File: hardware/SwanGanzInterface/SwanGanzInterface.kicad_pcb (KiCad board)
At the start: 2 copper layers, 27 parts, among them IC2 LM2937ET-3.3_NOPB, J1 2479774-1, Q1 SQ2389CES-T1_GE3, SW1 Power_Switch, U1 INA122D, U10 OPA2350, U2 OPA2350, U3 OPA2350, U4 INA122D, U5 OPA2350, U6 INA122D, U8 Adafruit ST7735R

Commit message: Footprints for most parts, added LCD Driver
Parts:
- added C1: 0.1u, Capacitor_SMD:C_0603_1608Metric, F.Cu at (250.4, 240.2)
- added C11: 0.1u, Capacitor_SMD:C_0603_1608Metric, F.Cu at (250.4, 228.2)
- added C12: 0.1u, Capacitor_SMD:C_1206_3216Metric, F.Cu at (267.8, 228.6)
- added C13: 0.1u, Capacitor_SMD:C_0603_1608Metric, F.Cu at (250.4, 230.7)
- added C15: 0.1u, Capacitor_SMD:C_1206_3216Metric, F.Cu at (255.2, 184.5)
- added C16: 0.1u, Capacitor_SMD:C_1206_3216Metric, F.Cu at (255.2, 187.8)
- added C17: 0.1u, Capacitor_SMD:C_0603_1608Metric, F.Cu at (250.4, 176.8)
- added C19: 0.1u, Capacitor_SMD:C_1206_3216Metric, F.Cu at (255.2, 206.5)
- added C2: 10u, Capacitor_SMD:C_1206_3216Metric, F.Cu at (255.2, 240.7)
- added C20: 0.1u, Capacitor_SMD:C_1206_3216Metric, F.Cu at (255.2, 209.9)
- added C21: 0.1u, Capacitor_SMD:C_0603_1608Metric, F.Cu at (250.4, 198.9)
- added C3: 0.1u, Capacitor_SMD:C_0603_1608Metric, F.Cu at (250.4, 242.8)
- added C4: 0.1u, Capacitor_SMD:C_0603_1608Metric, F.Cu at (95.7, 251.4)
- added C5: 0.1u, Capacitor_SMD:C_0603_1608Metric, F.Cu at (266.1, 140.6)
- added C6: 0.1u, Capacitor_SMD:C_0603_1608Metric, F.Cu at (95.7, 253.9)
- added C7: 0.1u, Capacitor_SMD:C_0603_1608Metric, F.Cu at (266.1, 143.1)
- added C8: 0.1u, Capacitor_SMD:C_0603_1608Metric, F.Cu at (221.3, 205.6)
- added C9: 0.1u, Capacitor_SMD:C_0603_1608Metric, F.Cu at (221.3, 208.1)
- added J2: Conn_01x08_Pin, Connector_PinHeader_2.54mm:PinHeader_1x08_P2.54mm_Vertical, F.Cu at (176.0, 75.3)
- added J3: Conn_01x03_Pin, Connector_PinHeader_2.54mm:PinHeader_1x03_P2.54mm_Vertical, F.Cu at (246.3, 145.0)
- added J6: Conn_01x04_Pin, Connector_PinSocket_2.54mm:PinSocket_1x04_P2.54mm_Vertical, F.Cu at (127.5, 223.5)
- added J7: Conn_01x04_Pin, Connector_PinSocket_2.54mm:PinSocket_1x04_P2.54mm_Vertical, F.Cu at (134.1, 223.5)
- added JP1: LP_3V3_Jumper, SGI_FootprintsLib:PinHeader_1x02_P2.54mm_Vertical, F.Cu at (221.6, 199.4)
- added JP2: LP_5V_Jumper, SGI_FootprintsLib:PinHeader_1x02_P2.54mm_Vertical, F.Cu at (226.3, 199.4)
- added JP3: FT232_3V3_Jumper, SGI_FootprintsLib:PinHeader_1x02_P2.54mm_Vertical, F.Cu at (230.9, 199.4)
- added R1: 5k1, Resistor_SMD:R_0603_1608Metric, F.Cu at (250.4, 245.3)
- added R10: 100R, Resistor_SMD:R_0603_1608Metric, F.Cu at (266.1, 148.1)
- added R11: 0R, Resistor_SMD:R_0603_1608Metric, F.Cu at (215.8, 209.7)
- added R12: 0R, Resistor_SMD:R_0603_1608Metric, F.Cu at (215.8, 212.2)
- added R13: 100k, Resistor_SMD:R_0603_1608Metric, F.Cu at (266.1, 150.7)
- added R14: 100R, Resistor_SMD:R_0603_1608Metric, F.Cu at (266.1, 153.2)
- added R15: 100k, Resistor_SMD:R_0603_1608Metric, F.Cu at (250.4, 233.2)
- added R16: 8k2, Resistor_SMD:R_0603_1608Metric, F.Cu at (250.4, 235.7)
- added R17: 100k, Resistor_SMD:R_0603_1608Metric, F.Cu at (254.4, 228.2)
- added R18: 65k5, Resistor_SMD:R_0603_1608Metric, F.Cu at (254.4, 230.7)
- added R19: 160k, Resistor_SMD:R_0603_1608Metric, F.Cu at (254.4, 233.2)
- added R2: 5k1, Resistor_SMD:R_0603_1608Metric, F.Cu at (250.4, 247.8)
- added R20: 160k, Resistor_SMD:R_0603_1608Metric, F.Cu at (254.4, 235.7)
- added R21: 10k, Resistor_SMD:R_0603_1608Metric, F.Cu at (258.4, 228.2)
- added R22: 10k, Resistor_SMD:R_0603_1608Metric, F.Cu at (258.4, 230.7)
- added R23: 10k, Resistor_SMD:R_0603_1608Metric, F.Cu at (258.4, 233.2)
- added R24: 10k, Resistor_SMD:R_0603_1608Metric, F.Cu at (258.4, 235.7)
- added R25: 200R, Resistor_SMD:R_0603_1608Metric, F.Cu at (250.4, 179.4)
- added R26: 32k, Resistor_SMD:R_0603_1608Metric, F.Cu at (250.4, 181.9)
- added R27: 32k, Resistor_SMD:R_0603_1608Metric, F.Cu at (250.4, 184.4)
- added R28: 10k, Resistor_SMD:R_0603_1608Metric, F.Cu at (250.4, 186.9)
- added R29: 50k, Resistor_SMD:R_0603_1608Metric, F.Cu at (250.4, 189.4)
- added R3: 47k, Resistor_SMD:R_0603_1608Metric, F.Cu at (250.4, 250.3)
- added R30: 10k, Resistor_SMD:R_0603_1608Metric, F.Cu at (250.4, 191.9)
- added R31: 10k, Resistor_SMD:R_0603_1608Metric, F.Cu at (250.4, 194.4)
- added R32: 200R, Resistor_SMD:R_0603_1608Metric, F.Cu at (250.4, 201.4)
- added R33: 32k, Resistor_SMD:R_0603_1608Metric, F.Cu at (250.4, 203.9)
- added R34: 32k, Resistor_SMD:R_0603_1608Metric, F.Cu at (250.4, 206.5)
- added R35: 10k, Resistor_SMD:R_0603_1608Metric, F.Cu at (250.4, 209.0)
- added R36: 50k, Resistor_SMD:R_0603_1608Metric, F.Cu at (250.4, 211.5)
- added R37: 10k, Resistor_SMD:R_0603_1608Metric, F.Cu at (250.4, 214.0)
- added R38: 10k, Resistor_SMD:R_0603_1608Metric, F.Cu at (250.4, 216.5)
- added R4: 10k, Resistor_SMD:R_0603_1608Metric, F.Cu at (250.4, 252.8)
- added R5: 1k, Resistor_SMD:R_0603_1608Metric, F.Cu at (250.4, 255.3)
- added R6: 5k, Resistor_SMD:R_0603_1608Metric, F.Cu at (221.3, 210.6)
- added R7: 5k, Resistor_SMD:R_0603_1608Metric, F.Cu at (221.3, 213.1)
- added R8: 5k, Resistor_SMD:R_0603_1608Metric, F.Cu at (221.3, 215.6)
- added R9: 100k, Resistor_SMD:R_0603_1608Metric, F.Cu at (266.1, 145.6)
- added TP10: TP, SGI_FootprintsLib:Testpoint_1x02_P2.54mm, F.Cu at (250.7, 222.1)
- added TP11: TP, SGI_FootprintsLib:Testpoint_1x02_P2.54mm, F.Cu at (255.3, 222.1)
- added TP12: TP, SGI_FootprintsLib:Testpoint_1x02_P2.54mm, F.Cu at (260.0, 222.1)
- added TP13: T_HG, SGI_FootprintsLib:Testpoint_1x02_P2.54mm, F.Cu at (269.3, 222.1)
- added TP14: T_LG, SGI_FootprintsLib:Testpoint_1x02_P2.54mm, F.Cu at (264.6, 222.1)
- added TP15: TP, SGI_FootprintsLib:Testpoint_1x02_P2.54mm, F.Cu at (254.7, 177.9)
- added TP16: TP, SGI_FootprintsLib:Testpoint_1x02_P2.54mm, F.Cu at (259.4, 177.9)
- added TP17: TP, SGI_FootprintsLib:Testpoint_1x02_P2.54mm, F.Cu at (264.0, 177.9)
- added TP18: P1_LG, SGI_FootprintsLib:Testpoint_1x02_P2.54mm, F.Cu at (268.7, 177.9)
- added TP19: P1_HG, SGI_FootprintsLib:Testpoint_1x02_P2.54mm, F.Cu at (273.3, 177.9)
- added TP20: TP, SGI_FootprintsLib:Testpoint_1x02_P2.54mm, F.Cu at (254.7, 200.0)
- added TP21: TP, SGI_FootprintsLib:Testpoint_1x02_P2.54mm, F.Cu at (259.4, 200.0)
- added TP22: TP, SGI_FootprintsLib:Testpoint_1x02_P2.54mm, F.Cu at (264.0, 200.0)
- added TP23: P2_LG, SGI_FootprintsLib:Testpoint_1x02_P2.54mm, F.Cu at (268.7, 200.0)
- added TP24: P2_HG, SGI_FootprintsLib:Testpoint_1x02_P2.54mm, F.Cu at (273.3, 200.0)
- added U2: LM4041CILPR, SGI_FootprintsLib:ti_LM4041CILPR, F.Cu at (223.6, 235.1)
- added U4: LP-MSPM0G3507, SGI_FootprintsLib:ti_LP_MSPM0G3507, B.Cu at (213.9, 77.3)
- added U7: FT232R, SGI_FootprintsLib:FT232R-Breakout, F.Cu at (269.5, 79.2)
- C10: renamed from C5; footprint Capacitor_SMD:C_0603_1608Metric -> Capacitor_SMD:C_1206_3216Metric
- moved C18 157.4 mm to (105.2, 237.5)
- moved J1 157.4 mm to (39.7, 261.8)
- moved Q1 157.4 mm to (71.9, 258.7)
- moved SW1 157.4 mm to (52.1, 266.2)
- moved U1 157.4 mm to (50.0, 260.4)
- moved U8 157.4 mm to (81.8, 264.5)
- moved C14 157.4 mm to (105.2, 216.8)
- moved D1 157.4 mm to (35.3, 243.5)
- moved D2 157.4 mm to (42.8, 243.5)
- moved D3 157.4 mm to (50.3, 243.5)
- moved U10 157.4 mm to (98.1, 219.1)
- moved U11 157.4 mm to (94.5, 205.9)
- moved U12 157.4 mm to (98.1, 239.8)
- moved U13 157.4 mm to (94.5, 226.6)
- moved U3 157.4 mm to (60.2, 258.5)
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- renumbered C10 to C14, C14 to C18, TP9 to TP5, TP5 to TP6, TP6 to TP7, TP7 to TP8, TP8 to TP9, IC2 to U1, U4 to U10, U5 to U11, U6 to U12, U10 to U13, U8 to U6, U1 to U8, U2 to U9
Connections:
- net Pres1AmpOut_LowGain renamed ADC_0.2
- net Pres2AmpOut_LowGain renamed ADC_1.3
- net ThermAmpOut_LowGain renamed ADC_0.5
- U10 pad 2: Net-(J2A-SIG-) -> P1_SIG-
- U10 pad 3: Net-(J2A-SIG+) -> P1_SIG+
- U10 pad 6: Net-(U4-OUT) -> P1__InstrOut
- U11 pad 7: Pres1AmpOut_HighGain -> ADC_0.3
- U12 pad 2: Net-(J3A-SIG-) -> P2_SIG-
- U12 pad 3: Net-(J3A-SIG+) -> P2_SIG+
- U12 pad 6: Net-(U6-OUT) -> P2__InstrOut
- U13 pad 7: Pres2AmpOut_HighGain -> ADC_1.5
- U6 pad 10: Net-(U8-LITE) -> +3V3
- U6 pad 3: unconnected-(U8-RESET-Pad3) -> PB15
- U6 pad 4: unconnected-(U8-D/C-Pad4) -> PB16
- U6 pad 5: unconnected-(U8-CARD_CS-Pad5) -> PB0
- U6 pad 6: unconnected-(U8-TFT_CS-Pad6) -> PB6
- U6 pad 7: unconnected-(U8-MOSI-Pad7) -> PB8
- U6 pad 8: unconnected-(U8-SCK-Pad8) -> PB9
- U6 pad 9: unconnected-(U8-MISO-Pad9) -> PB7
- U8 pad 6: Net-(U1-OUT) -> Therm__InstrOut
- U9 pad 7: ThermAmpOut_HighGain -> ADC_0.7

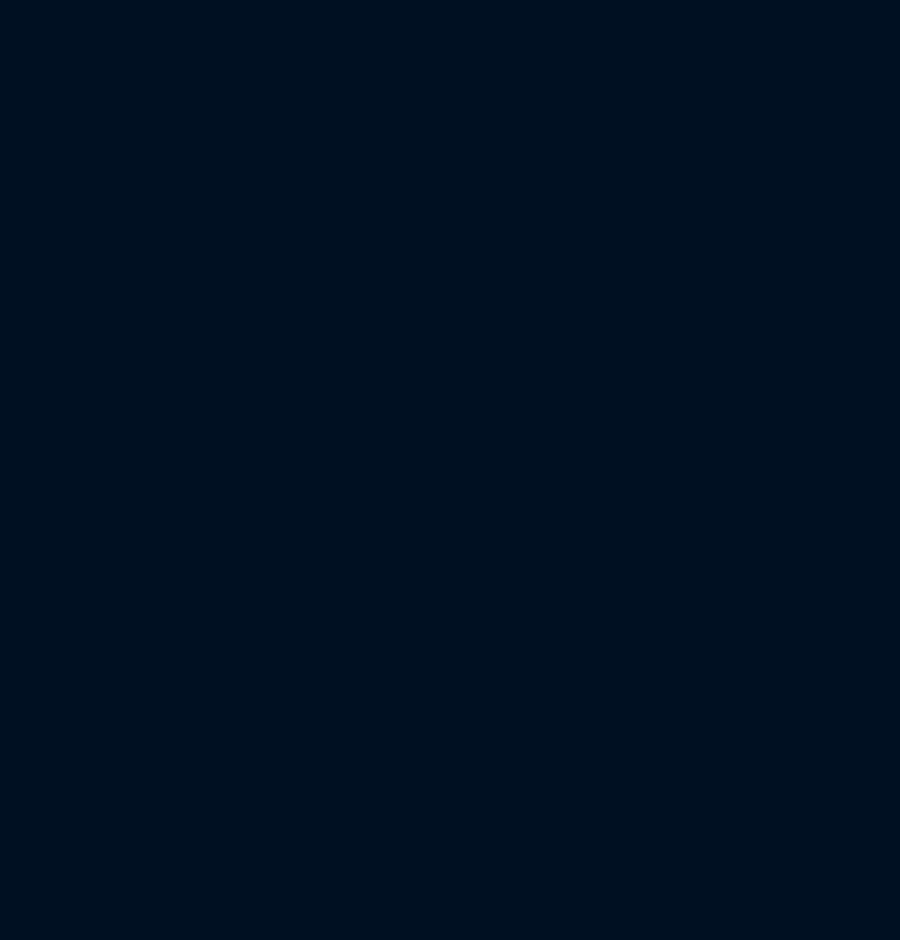
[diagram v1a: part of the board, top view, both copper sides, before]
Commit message: Consolidated Grounds
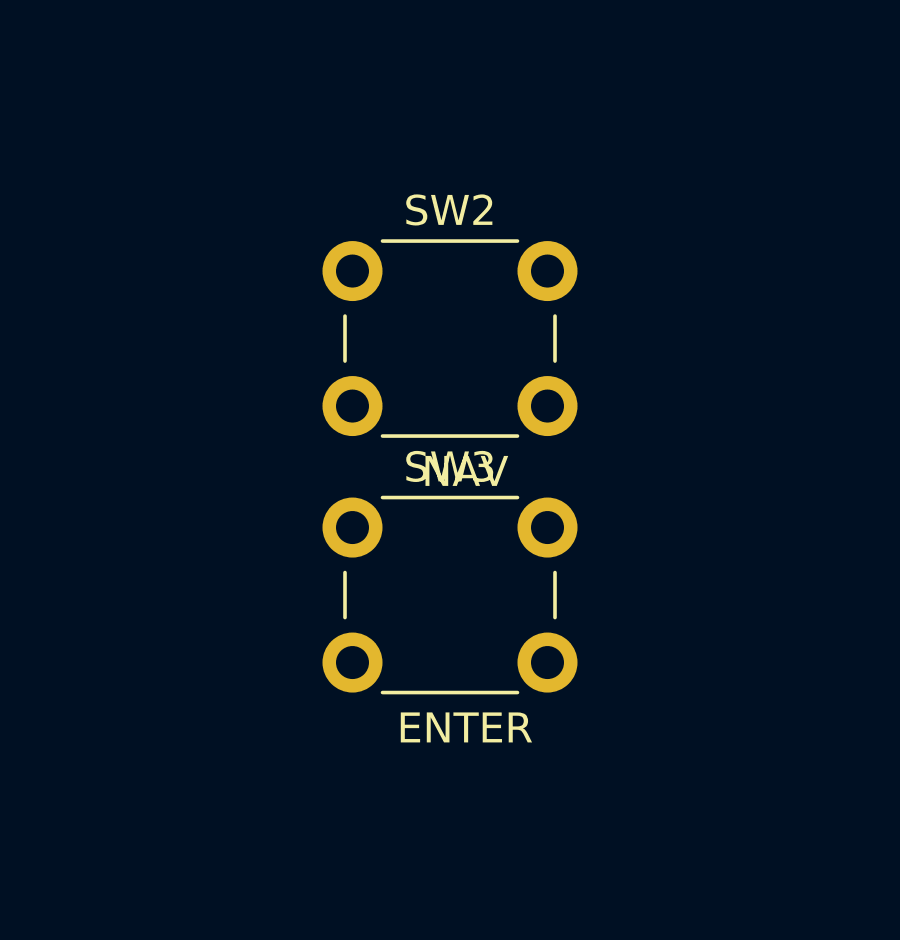
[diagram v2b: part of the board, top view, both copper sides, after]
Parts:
- added SW2: NAV, SGI_FootprintsLib:SW_PUSH_6mm, F.Cu at (164.2, 153.6)
- added SW3: ENTER, SGI_FootprintsLib:SW_PUSH_6mm, F.Cu at (164.2, 162.1)
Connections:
- C14 pad 1: AGND -> GND
- C18 pad 1: AGND -> GND
- TP6 pad 1: DGND -> GND
- TP6 pad 2: DGND -> GND
- TP7 pad 1: AGND -> GND
- TP7 pad 2: AGND -> GND
- TP8 pad 1: DGND -> GND
- TP8 pad 2: DGND -> GND
- TP9 pad 1: AGND -> GND
- TP9 pad 2: AGND -> GND
- U8 pad 5: AGND -> GND

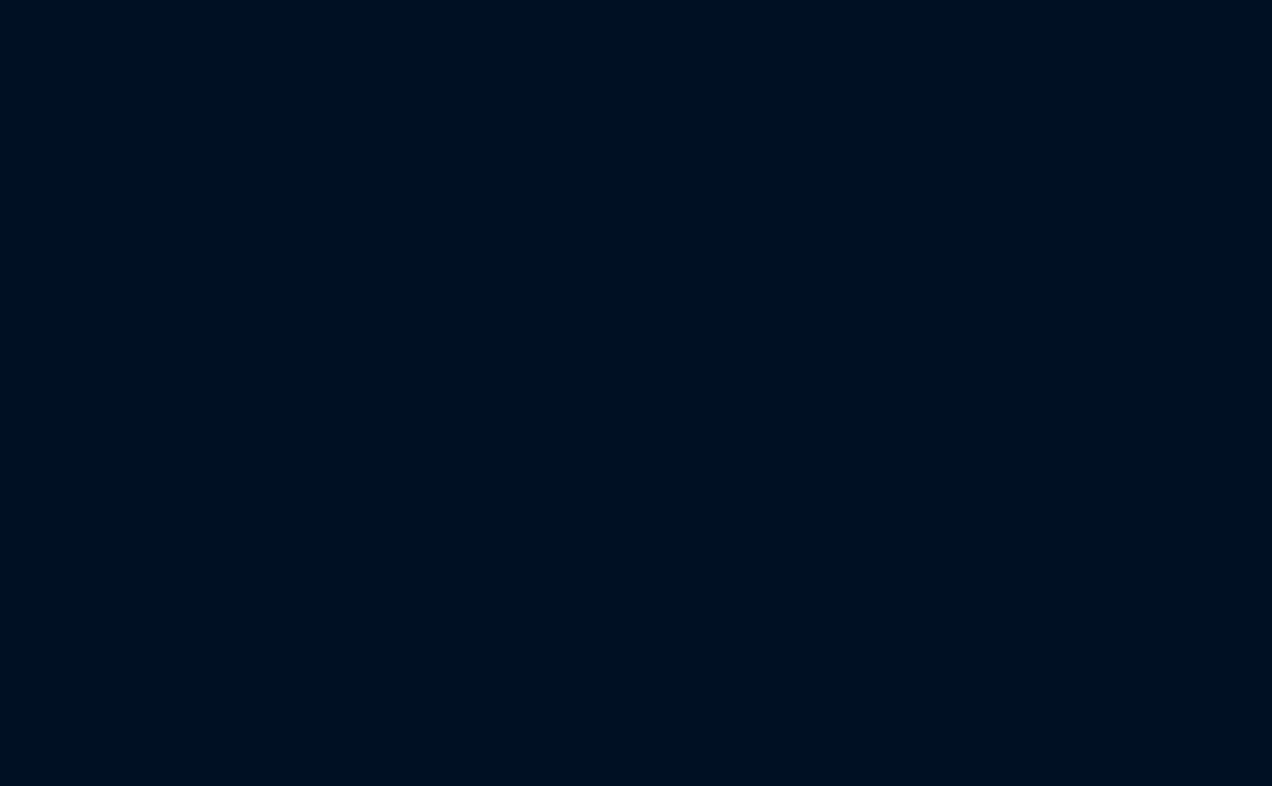
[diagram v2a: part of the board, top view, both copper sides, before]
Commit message: Added footprint and linked to connector symbol
PCB layout also updated with new footprint.
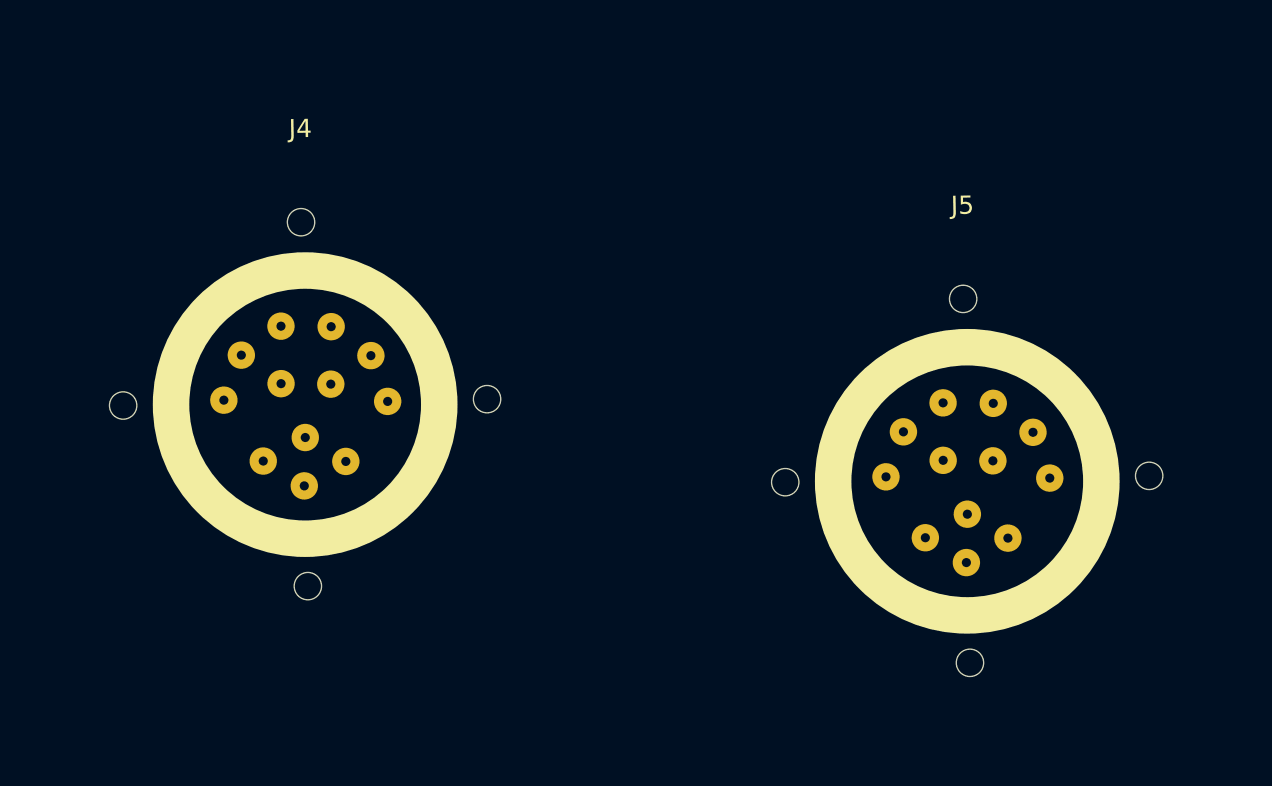
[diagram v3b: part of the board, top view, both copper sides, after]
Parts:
- added J4: ~, Connectors:Pressure_Connector, F.Cu at (101.5, 87.0)
- added J5: ~, Connectors:Pressure_Connector, F.Cu at (137.8, 91.2)
